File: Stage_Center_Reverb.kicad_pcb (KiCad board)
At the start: 2 copper layers, 75 x 50 mm, 43 parts, among them J10 Power, J2 Output, J3 Tank, SW2 kill, U1 TL072, U10 L78L15, U11 L79L15, U2 TL072

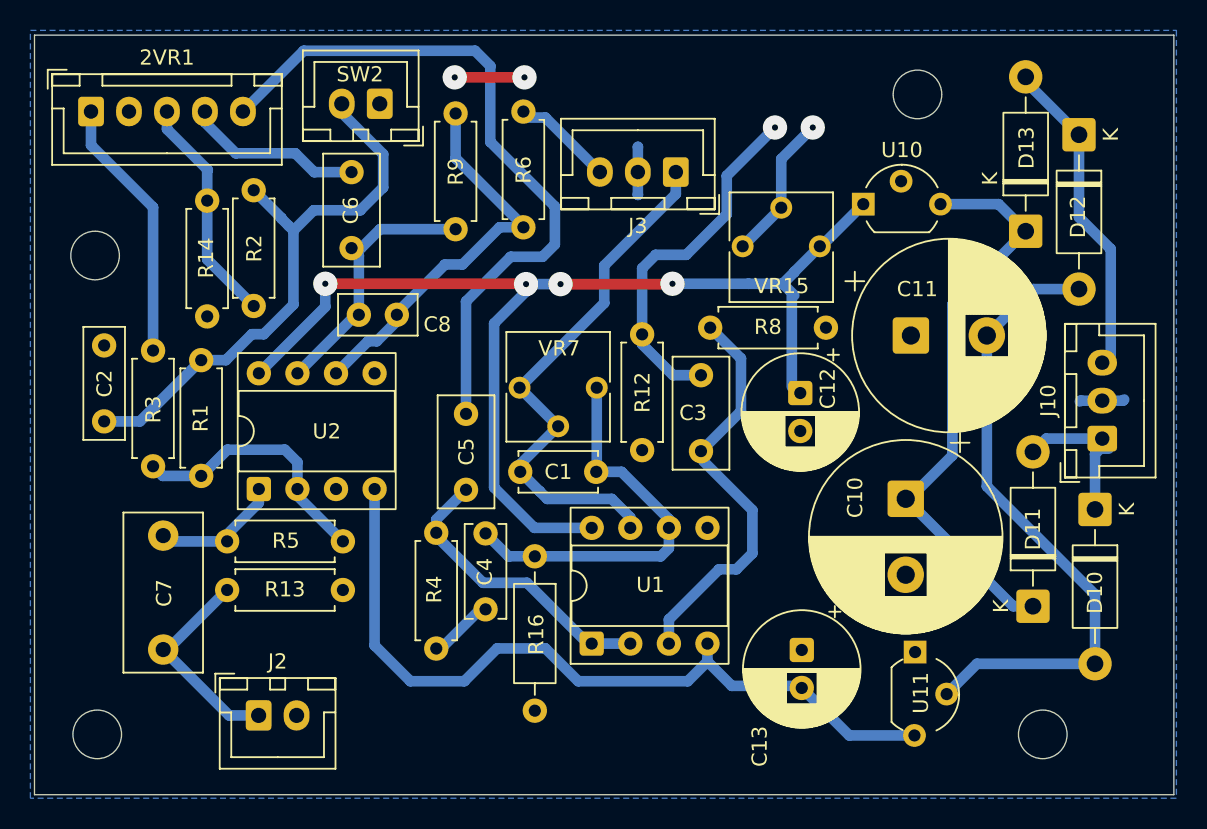
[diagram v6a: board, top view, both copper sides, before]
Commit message: 全体ではなく外周をGNDで囲むように変更
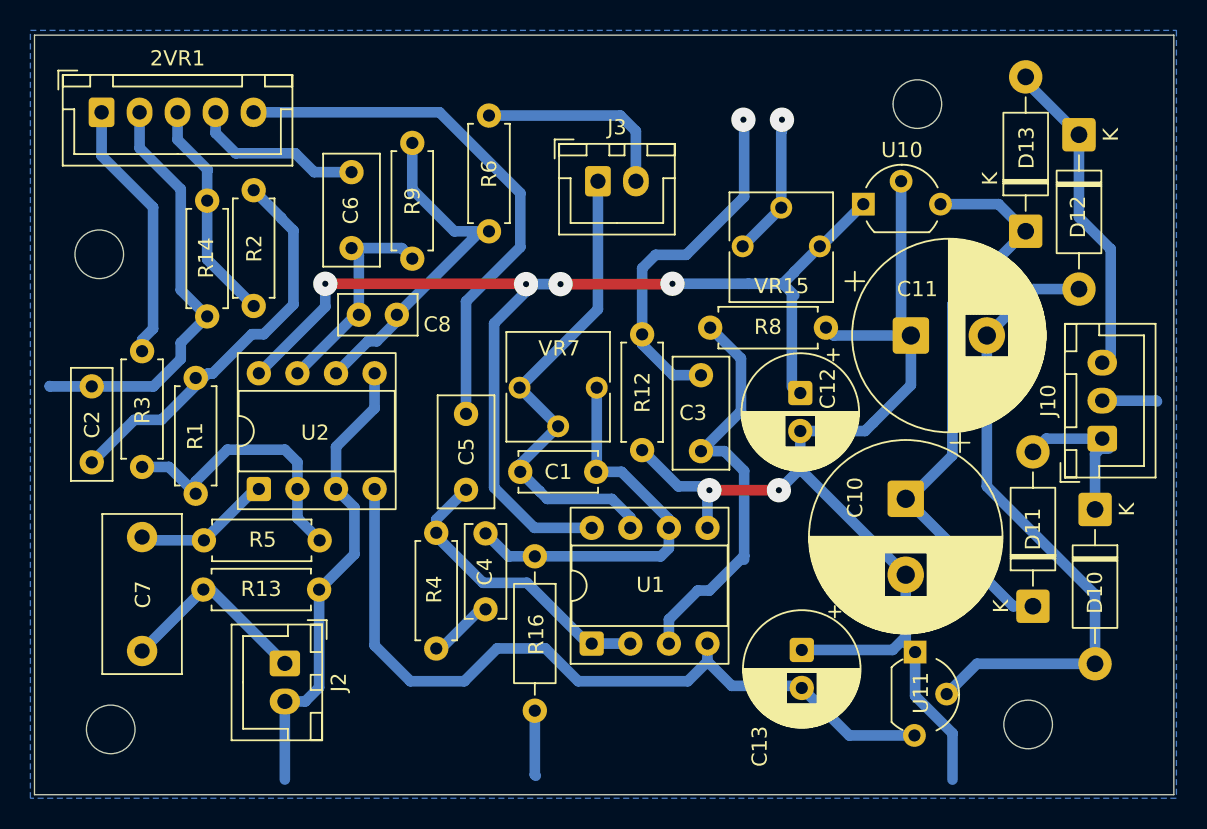
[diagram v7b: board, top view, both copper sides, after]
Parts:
- removed SW2: kill, Connector_JST:JST_XH_B2B-XH-A_1x02_P2.50mm_Vertical
- J3: footprint Connector_JST:JST_XH_B3B-XH-A_1x03_P2.50mm_Vertical -> Connector_JST:JST_XH_B2B-XH-A_1x02_P2.50mm_Vertical
- moved J3 5.16 mm to (130.6, 86.1), turned to 0 degrees
- moved J2 3.83 mm to (110.0, 117.8), turned to -90 degrees
- moved R9 3.45 mm to (118.4, 91.2)
- moved C2 2.82 mm to (97.3, 104.6)
- moved R6 2.28 mm to (123.4, 89.4)
- moved R13 1.57 mm to (104.6, 113.0)
- moved R5 1.53 mm to (104.6, 109.7)
- moved C7 1.39 mm to (100.6, 109.5)
- moved R1 1.23 mm to (104.1, 106.7)
- moved H4 1.16 mm to (158.9, 121.8)
- moved H3 0.95 mm to (98.5, 122.2)
- moved R3 0.72 mm to (100.6, 104.9)
- moved 2VR1 0.70 mm to (97.9, 81.6)
- moved H2 0.64 mm to (151.6, 81.0)
- moved H1 0.29 mm to (97.8, 90.9)
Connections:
- J3 pad 2: GNDPWR -> Net-(J3-Pin_2)
- R6 pad 2: Net-(J3-Pin_3) -> Net-(J3-Pin_2)
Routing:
- net GNDPWR: track 13.5 -> 144.9 mm
- net Net-(J3-Pin_2): track 0.00 -> 13.4 mm
- net Net-(SW2-B): track 38.0 -> 26.2 mm
- net Net-(2VR1-Pad1): track 46.7 -> 35.8 mm
- net Net-(J3-Pin_3): track 6.50 -> 0.00 mm
- net Net-(C6-Pad1): track 17.8 -> 14.7 mm
- net Net-(J3-Pin_1): track 35.4 -> 32.7 mm
- net Net-(U2B--): track 25.9 -> 23.8 mm
- net Net-(U2A--): track 17.3 -> 18.7 mm
- net Net-(U1A-+): track 26.4 -> 27.6 mm
- net Net-(D1-A): track 9.80 -> 8.65 mm
- net Net-(SW1a1-B): track 23.8 -> 22.7 mm
- net Net-(J2-Pin_1): track 13.9 -> 13.1 mm

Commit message: ラインを0.4、パッドやビアを直径 2 2、ドリル穴を0.4に
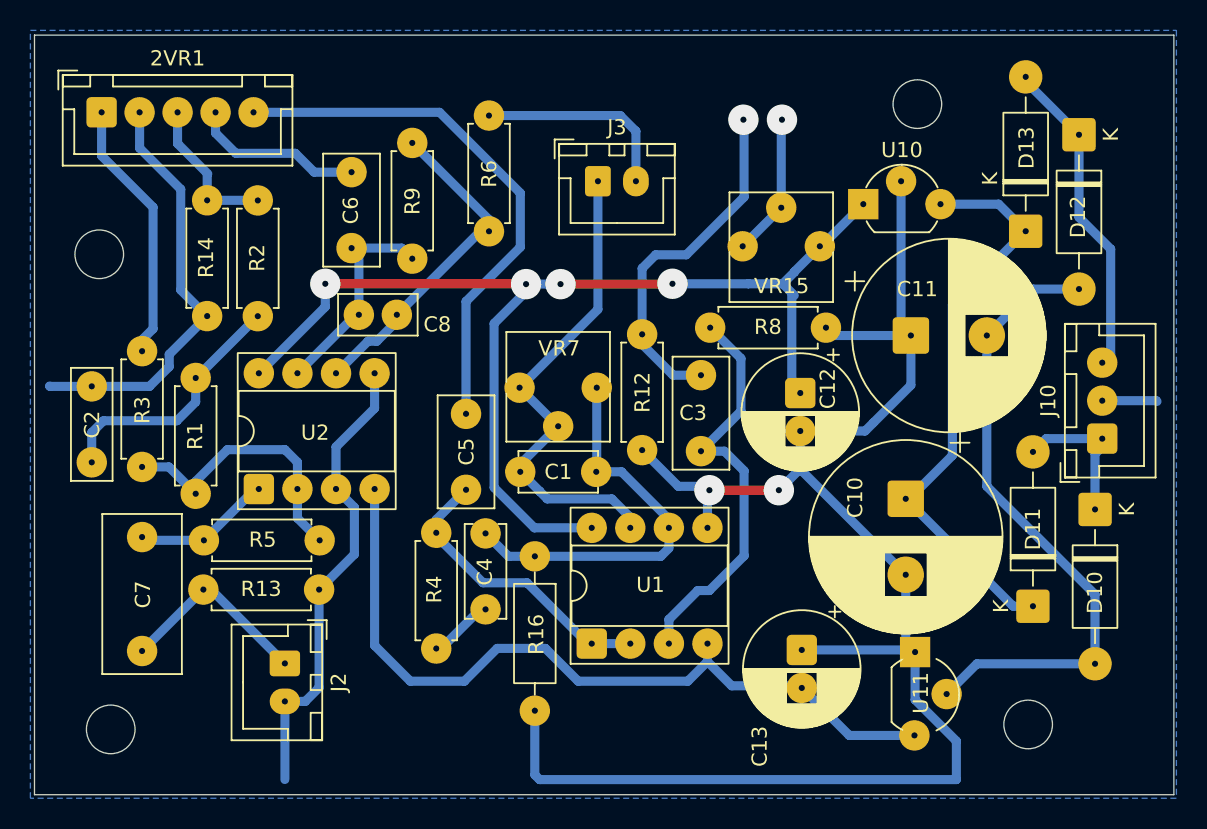
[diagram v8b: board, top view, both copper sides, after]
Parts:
- moved R2 8.30 mm to (108.2, 95.0), turned to 90 degrees
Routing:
- net GNDPWR: track 144.9 -> 173.0 mm
- net Net-(C2-Pad1): track 26.2 -> 17.0 mm
- net Net-(2VR1-Pad5): track 14.9 -> 9.94 mm
- net Net-(U2B--): track 23.8 -> 22.2 mm
